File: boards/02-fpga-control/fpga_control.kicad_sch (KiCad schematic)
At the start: 2 parts, among them J1 CONN_DF40_100P_M, J2 CONN_DF40_100P_F

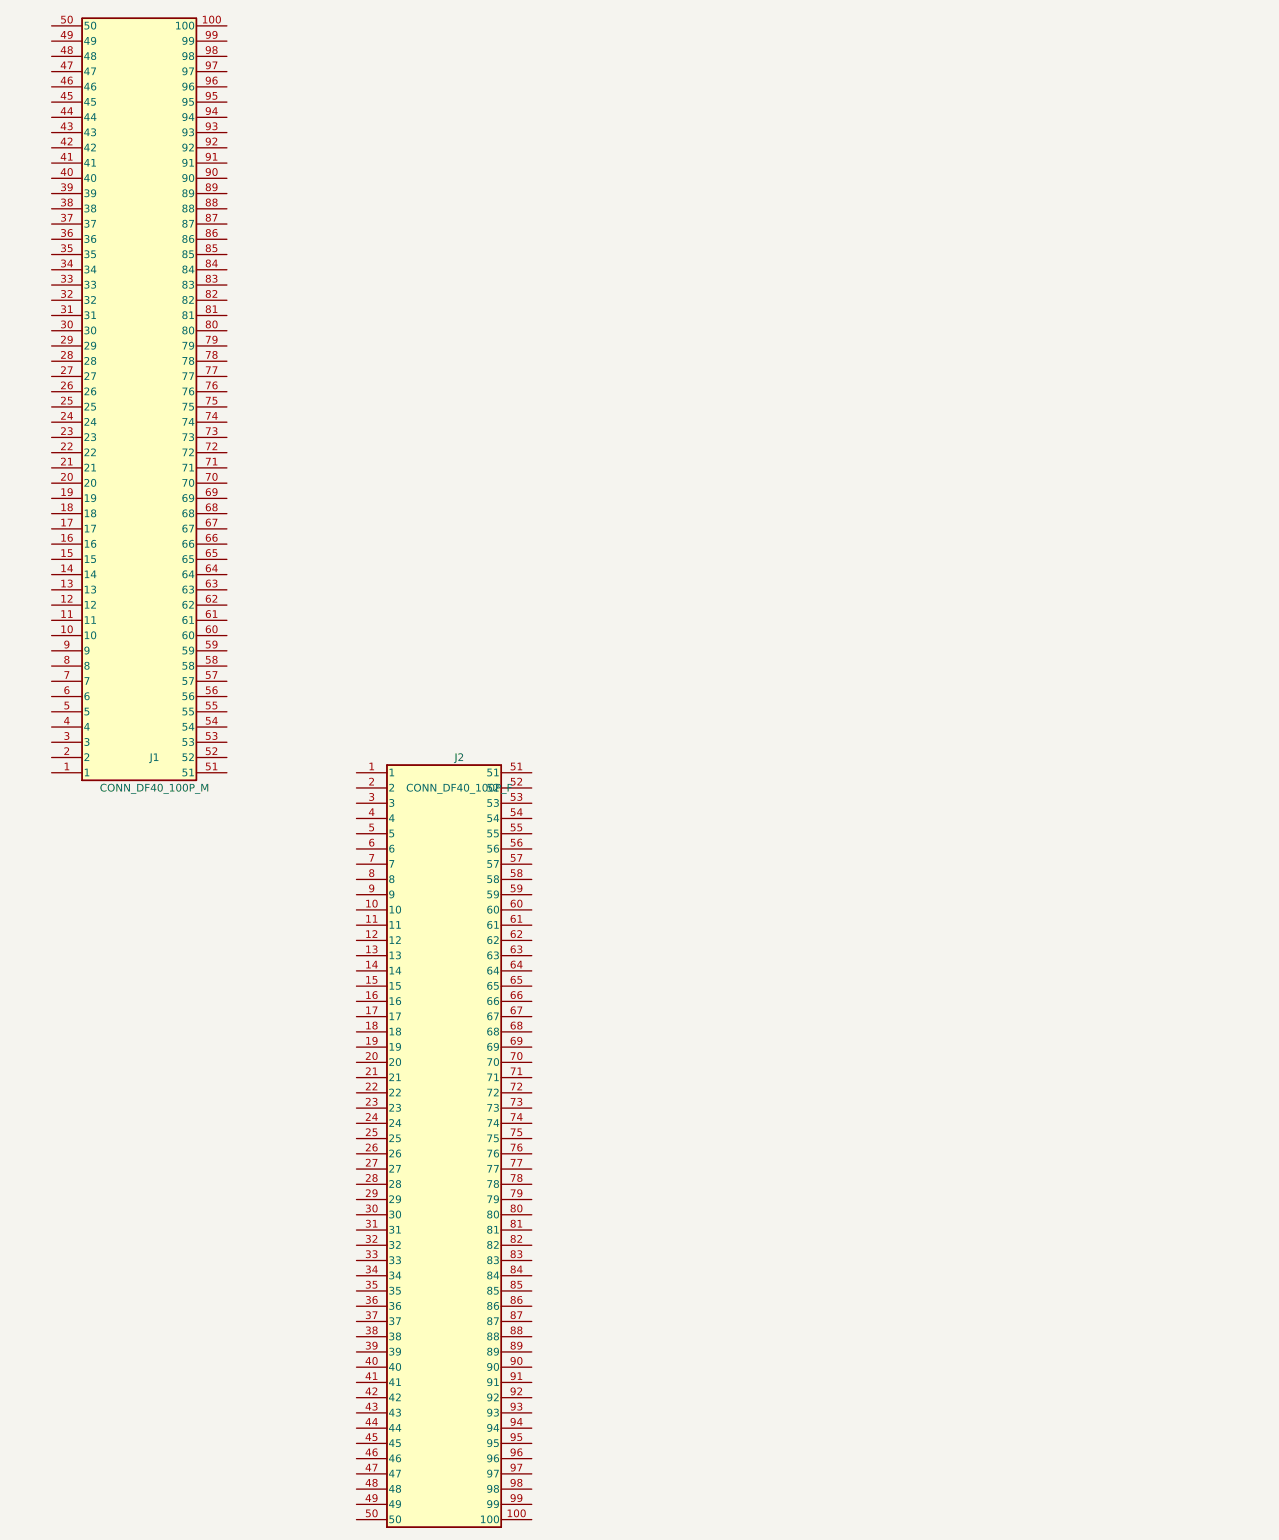
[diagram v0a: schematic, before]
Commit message: Update connector pinout
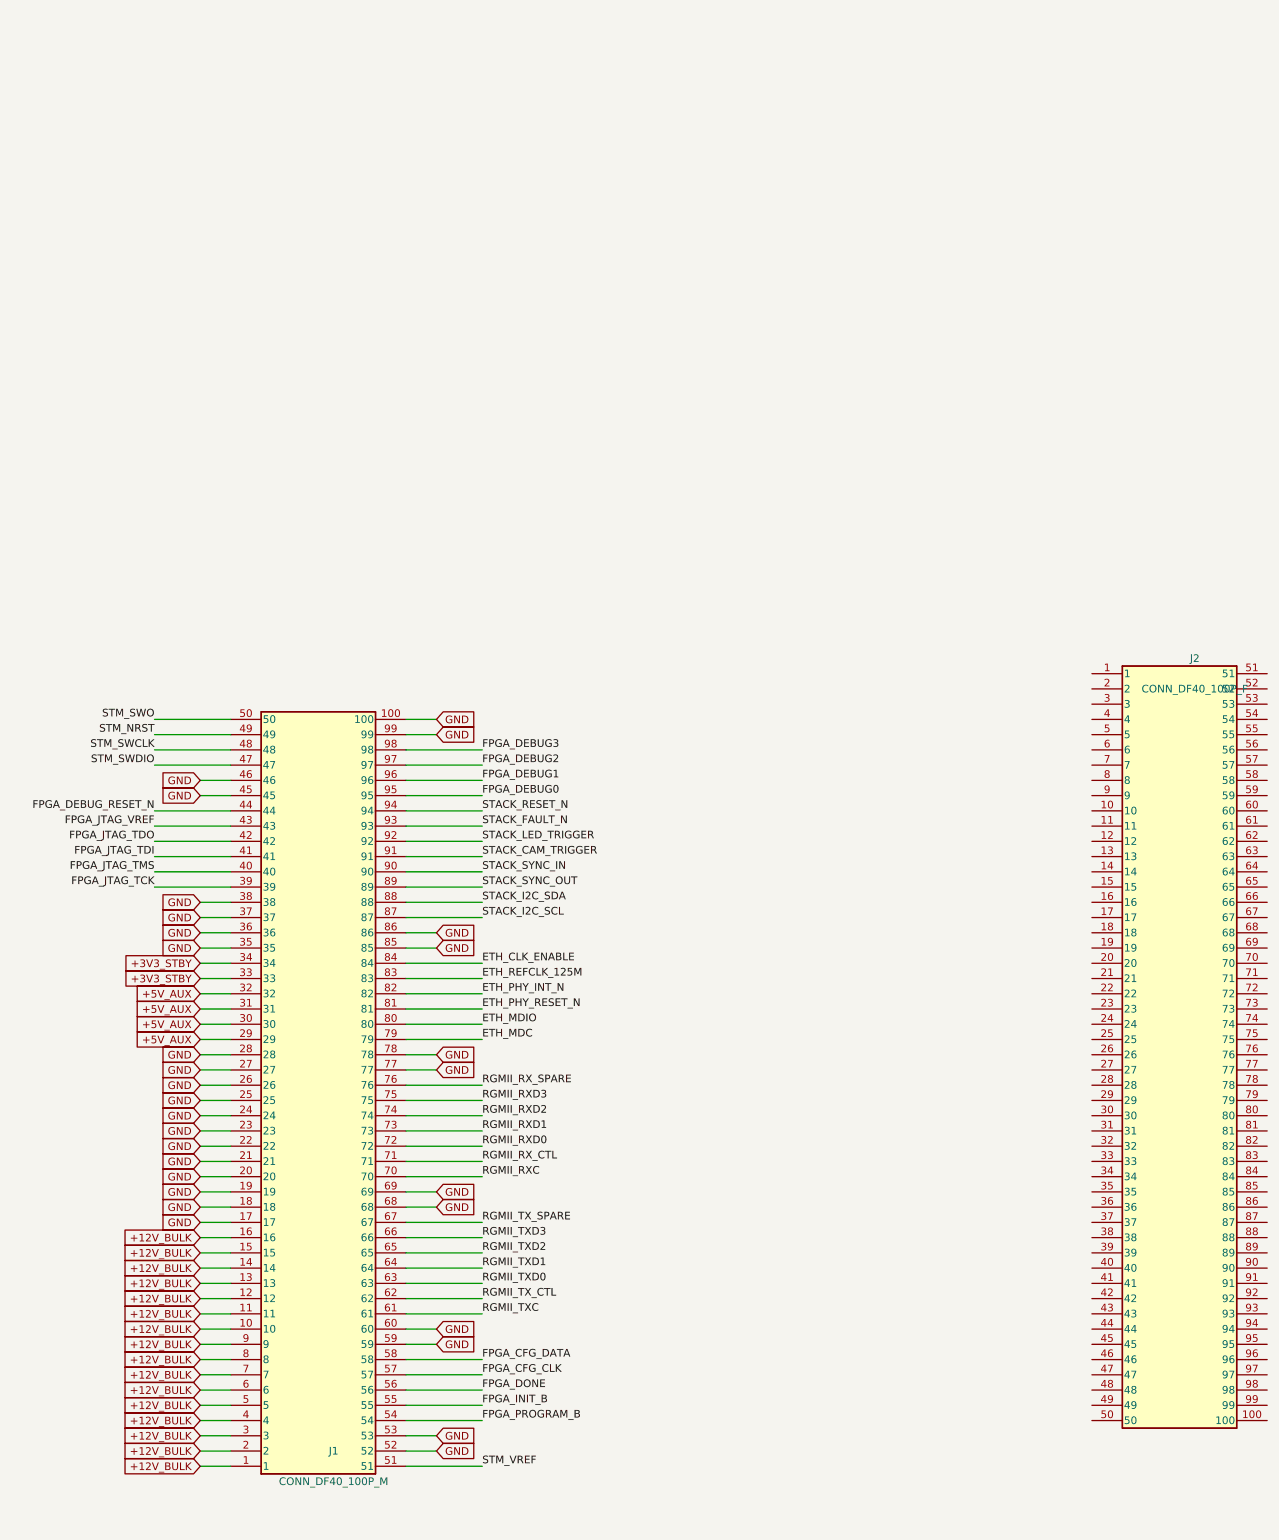
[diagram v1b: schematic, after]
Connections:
- net +12V_BULK: now reaches J1.1
- net +12V_BULK: now also J1.10, J1.11, J1.12, J1.13, J1.14, J1.15, J1.16, J1.2, J1.3, J1.4, J1.5, J1.6, J1.7, J1.8, J1.9
- net GND: now reaches J1.100
- net GND: now also J1.17, J1.18, J1.19, J1.20, J1.21, J1.22, J1.23, J1.24, J1.25, J1.26, J1.27, J1.28, J1.35, J1.36, J1.37, J1.38, J1.45, J1.46, J1.52, J1.53, J1.59, J1.60, J1.68, J1.69, J1.77, J1.78, J1.85, J1.86, J1.99
- net +5V_AUX: now reaches J1.29
- net +5V_AUX: now also J1.30, J1.31, J1.32
- net +3V3_STBY: now reaches J1.33
- net +3V3_STBY: now also J1.34
- net FPGA_JTAG_TCK: now reaches J1.39
- net FPGA_JTAG_TMS: now reaches J1.40
- net FPGA_JTAG_TDI: now reaches J1.41
- net FPGA_JTAG_TDO: now reaches J1.42
- net FPGA_JTAG_VREF: now reaches J1.43
- net FPGA_DEBUG_RESET_N: now reaches J1.44
- net STM_SWDIO: now reaches J1.47
- net STM_SWCLK: now reaches J1.48
- net STM_NRST: now reaches J1.49
- net STM_SWO: now reaches J1.50
- net STM_VREF: now reaches J1.51
- net FPGA_PROGRAM_B: now reaches J1.54
- net FPGA_INIT_B: now reaches J1.55
- net FPGA_DONE: now reaches J1.56
- net FPGA_CFG_CLK: now reaches J1.57
- net FPGA_CFG_DATA: now reaches J1.58
- net RGMII_TXC: now reaches J1.61
- net RGMII_TX_CTL: now reaches J1.62
- net RGMII_TXD0: now reaches J1.63
- net RGMII_TXD1: now reaches J1.64
- net RGMII_TXD2: now reaches J1.65
- net RGMII_TXD3: now reaches J1.66
- net RGMII_TX_SPARE: now reaches J1.67
- net RGMII_RXC: now reaches J1.70
- net RGMII_RX_CTL: now reaches J1.71
- net RGMII_RXD0: now reaches J1.72
- net RGMII_RXD1: now reaches J1.73
- net RGMII_RXD2: now reaches J1.74
- net RGMII_RXD3: now reaches J1.75
- net RGMII_RX_SPARE: now reaches J1.76
- net ETH_MDC: now reaches J1.79
- net ETH_MDIO: now reaches J1.80
- net ETH_PHY_RESET_N: now reaches J1.81
- net ETH_PHY_INT_N: now reaches J1.82
- net ETH_REFCLK_125M: now reaches J1.83
- net ETH_CLK_ENABLE: now reaches J1.84
- net STACK_I2C_SCL: now reaches J1.87
- net STACK_I2C_SDA: now reaches J1.88
- net STACK_SYNC_OUT: now reaches J1.89
- net STACK_SYNC_IN: now reaches J1.90
- net STACK_CAM_TRIGGER: now reaches J1.91
- net STACK_LED_TRIGGER: now reaches J1.92
- net STACK_FAULT_N: now reaches J1.93
- net STACK_RESET_N: now reaches J1.94
- net FPGA_DEBUG0: now reaches J1.95
- net FPGA_DEBUG1: now reaches J1.96
- net FPGA_DEBUG2: now reaches J1.97
- net FPGA_DEBUG3: now reaches J1.98
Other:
- moved on the sheet: J1, J2
